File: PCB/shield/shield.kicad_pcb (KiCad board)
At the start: 2 copper layers, 128.2 x 80.1 mm, 19 parts, among them J1 QTR-8A, J10 ESP32_left_m, J11 ESP32_right_m, J13 Conn_01x06, J14 Domino, J15 Domino, J2 QMC5883L, J3 Servo, J4 Domino, J5 Joystick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

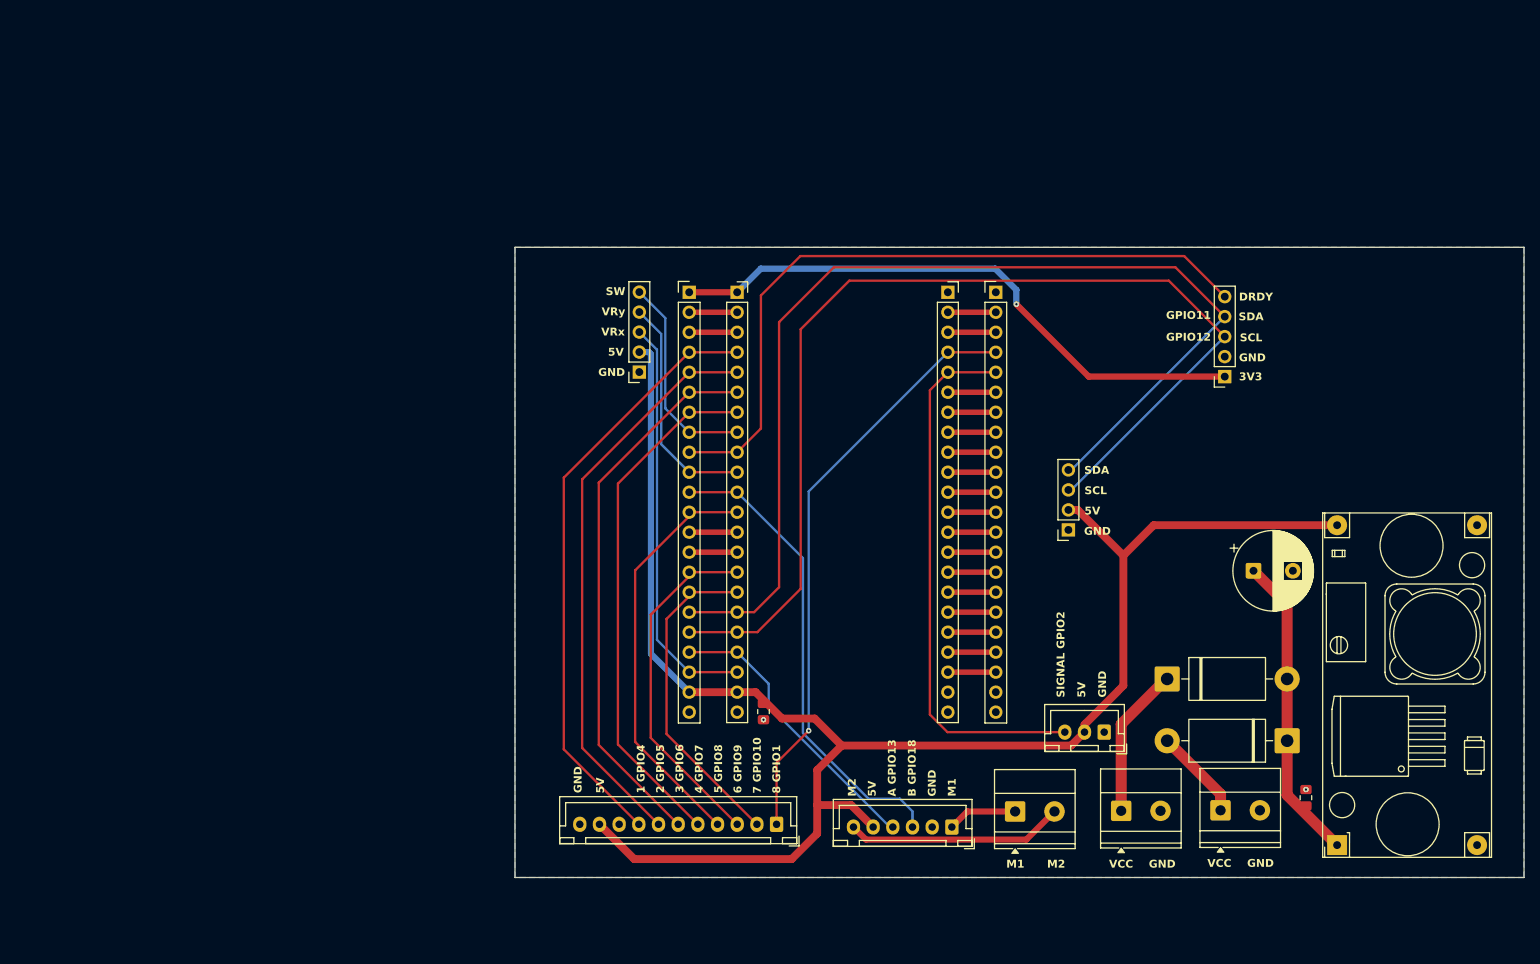
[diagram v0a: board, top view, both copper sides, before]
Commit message: feat: make pcb smaller
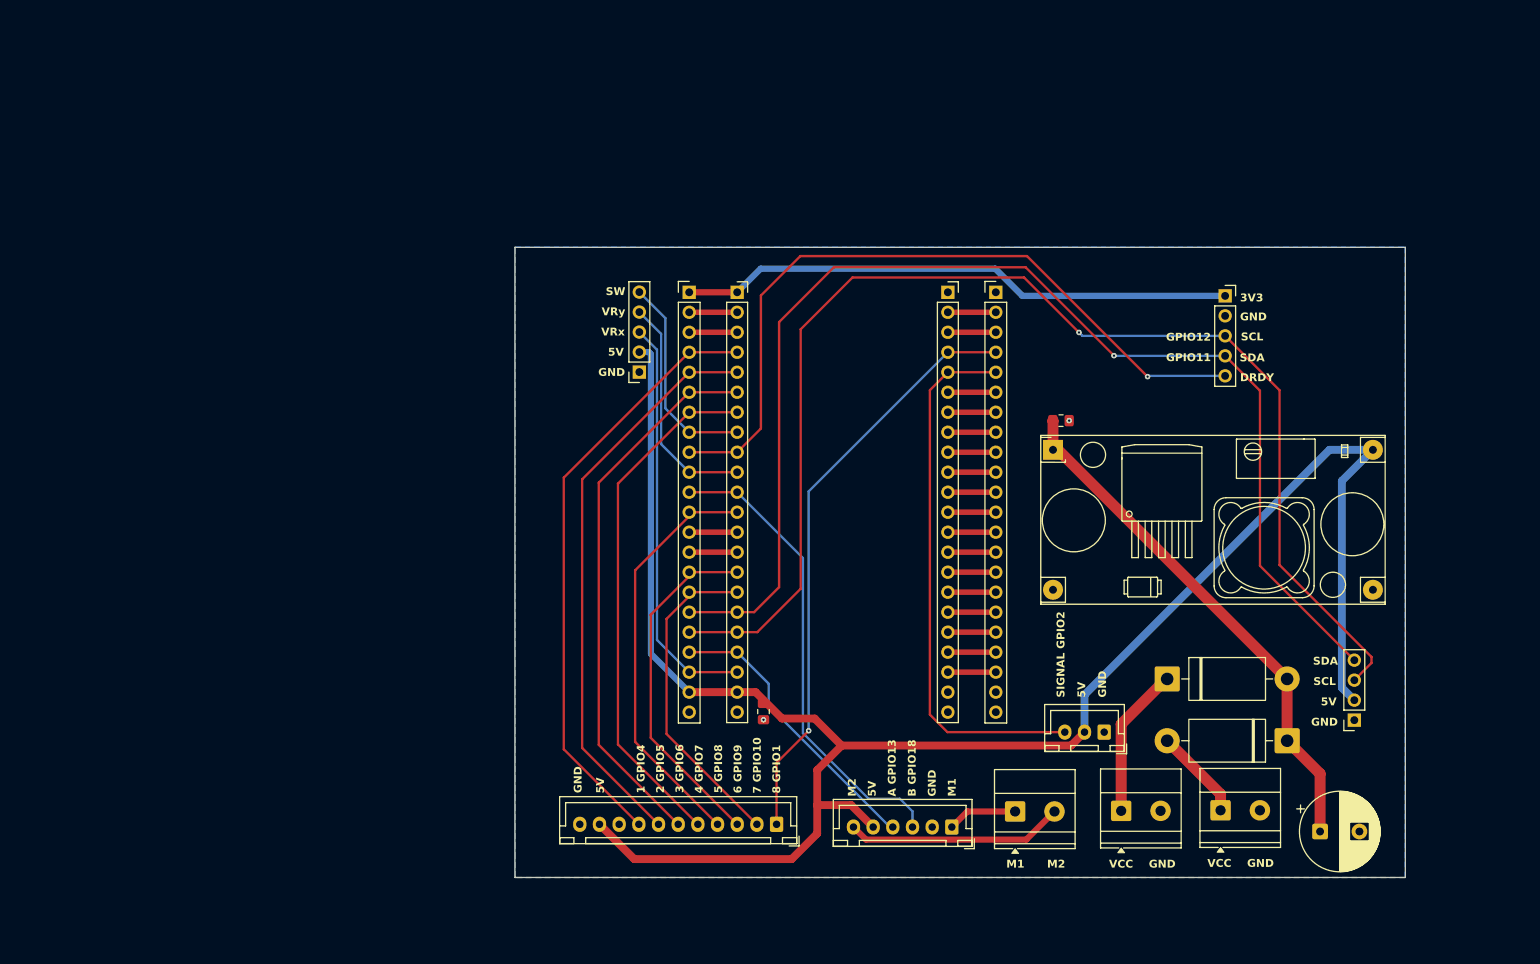
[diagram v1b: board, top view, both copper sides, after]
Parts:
- moved U1 61.8 mm to (155.9, 92.7), turned to 0 degrees
- moved C3 57.1 mm to (156.9, 89.0), turned to 0 degrees
- moved J6 43.6 mm to (194.2, 127.1)
- moved C1 34.2 mm to (189.9, 141.2)
- moved J2 10.3 mm to (177.8, 73.2), turned to 0 degrees
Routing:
- net VCC: track 39.2 -> 66.6 mm
- net +5V: track 214.2 -> 240.2 mm
- net /GPIO12+SCL: track 136.3 -> 161.5 mm, vias 0 -> 1
- net /GPIO11+SDA: track 136.1 -> 156.1 mm, vias 0 -> 1
- net +3V3: track 76.0 -> 70.8 mm, vias 1 -> 0
- net /GPIO16: track 90.4 -> 94.7 mm, vias 0 -> 1
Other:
- board size 128.2 x 80.1 mm -> 113.1 x 80.1 mm

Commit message: wip: commit to change workplace
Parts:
- removed J10: ESP32_left_m, Connector_PinHeader_2.54mm:PinHeader_1x22_P2.54mm_Vertical
- removed J11: ESP32_right_m, Connector_PinHeader_2.54mm:PinHeader_1x22_P2.54mm_Vertical
- removed J8: ESP32_left_f, Connector_PinSocket_2.54mm:PinSocket_1x22_P2.54mm_Vertical
- removed J9: ESP32_right_f, Connector_PinSocket_2.54mm:PinSocket_1x22_P2.54mm_Vertical
- added J7: L298N, Connector_JST:JST_XH_B3B-XH-A_1x03_P2.50mm_Vertical, F.Cu at (189.6, 76.3)
- added U2: ESP32-S3-DevKitC, PCM_Espressif:ESP32-S3-DevKitC, F.Cu at (156.8, 124.1)
- C3, C5: footprint Capacitor_SMD:C_0805_2012Metric_Pad1.18x1.45mm_HandSolder -> Capacitor_THT:CP_Radial_D5.0mm_P2.50mm
- moved C5 76.5 mm to (165.1, 64.9), turned to 0 degrees
- moved J6 63.9 mm to (187.5, 63.5), turned to 0 degrees
- moved J14 61.2 mm to (191.4, 92.6), turned to 90 degrees
- moved J5 55.4 mm to (127.7, 132.6), turned to 0 degrees
- moved J13 54.0 mm to (188.6, 111.6), turned to 90 degrees
- moved J1 49.0 mm to (169.8, 141.9)
- moved J2 45.8 mm to (187.4, 118.0), turned to 90 degrees
- moved C3 30.3 mm to (167.9, 117.3), turned to 180 degrees
- moved J3 27.8 mm to (138.0, 141.8)
- moved C1 24.3 mm to (171.0, 125.8), turned to 180 degrees
- moved U1 20.5 mm to (165.1, 111.0), turned to 90 degrees
- moved J15 14.1 mm to (178.6, 139.3)
- moved J4 13.6 mm to (190.8, 139.4)
- moved D2 11.2 mm to (178.1, 130.0)
- moved D1 10.0 mm to (193.5, 123.4)
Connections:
- net Net-(J13-Pin_1) renamed /M1
- net Net-(J13-Pin_6) renamed /M2
- D1 pad 1: VCC -> Net-(D1-K)
- D1 pad 2: Net-(D1-A) -> VCC
- D2 pad 1: Net-(D2-K) -> VCC
- D2 pad 2: VCC -> Net-(D2-A)
- J1 pad 1: /GPIO1 -> /GPIO4
- J1 pad 2: /GPIO10 -> /GPIO5
- J1 pad 3: /GPIO9 -> /GPIO6
- J1 pad 4: /GPIO8 -> /GPIO7
- J1 pad 5: /GPIO7 -> /GPIO8
- J1 pad 6: /GPIO6 -> /GPIO3
- J1 pad 7: /GPIO5 -> /GPIO9
- J1 pad 8: /GPIO4 -> /GPIO10
- J13 pad 3: /GPIO18 -> /GPIO17
- J13 pad 4: /GPIO13 -> /GPIO18
- J15 pad 1: Net-(D2-K) -> Net-(D1-K)
- J2 pad 3: /GPIO12+SCL -> /GPIO15
- J2 pad 4: /GPIO11+SDA -> /GPIO16
- J2 pad 5: /GPIO16 -> unconnected-(J2-Pin_5-Pad5)
- J3 pad 3: /GPIO2 -> /GPIO11
- J4 pad 1: Net-(D1-A) -> Net-(D2-A)
- J5 pad 3: /GPIO14 -> /GPIO2
- J5 pad 4: /GPIO17 -> /GPIO1
- J5 pad 5: /GPIO15 -> /GPIO12
- J6 pad 3: /GPIO12+SCL -> /GPIO15
- J6 pad 4: /GPIO11+SDA -> /GPIO16
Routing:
- net /GPIO12+SCL: track 161.5 -> 0.00 mm, vias 1 -> 0
- net /GPIO11+SDA: track 156.1 -> 0.00 mm, vias 1 -> 0
- net /GPIO15: track 26.5 -> 107.4 mm
- net /GPIO12: track 0.00 -> 76.9 mm
- net /GPIO11: track 0.00 -> 71.1 mm
- net /GPIO21: track 0.00 -> 56.8 mm
- net /GPIO3: track 0.00 -> 54.6 mm
- net /GPIO1: track 75.1 -> 26.3 mm, vias 1 -> 0
- net /GPIO4: track 76.6 -> 32.8 mm
- net /GPIO2: track 68.6 -> 26.3 mm
- net /GPIO5: track 73.2 -> 35.1 mm
- net VCC: track 66.6 -> 32.2 mm
- net /GPIO6: track 69.9 -> 37.4 mm
- net /GPIO7: track 66.4 -> 39.8 mm
- net /GPIO18: track 60.2 -> 34.0 mm
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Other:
- board size 113.1 x 80.1 mm -> 79.7 x 87.2 mm
- board text added: "1"
- board text added: "2"
- board text added: "3"
- board text added: "4"
- board text added: "5"
- board text added: "6"
- board text added: "7"
- board text added: "8"
- board text added: "A"
- board text added: "B"
- board text added: "EN"
- board text added: "IN1"
- board text added: "IN2"
- board text added: "JOYSTICK"
- board text added: "L298N"
- board text added: "MOTOR"
- board text added: "QMC5883L"
- board text added: "QTR-8A"
- board text added: "SCREEN"
- board text added: "SERVO"
- board text added: "SIGNAL"
- board text added: "Vin"
- board text added: "Vout"
- board text removed: "1 GPIO4"
- board text removed: "2 GPIO5"
- board text removed: "3 GPIO6"
- board text removed: "4 GPIO7"
- board text removed: "5 GPIO8"
- board text removed: "6 GPIO9"
- board text removed: "7 GPIO10"
- board text removed: "8 GPIO1"
- board text removed: "A GPIO13"
- board text removed: "B GPIO18"
- board text removed: "DRDY"
- board text removed: "GPIO11"
- board text removed: "GPIO12"
- board text removed: "SIGNAL GPIO2"
- board text removed: "VCC"

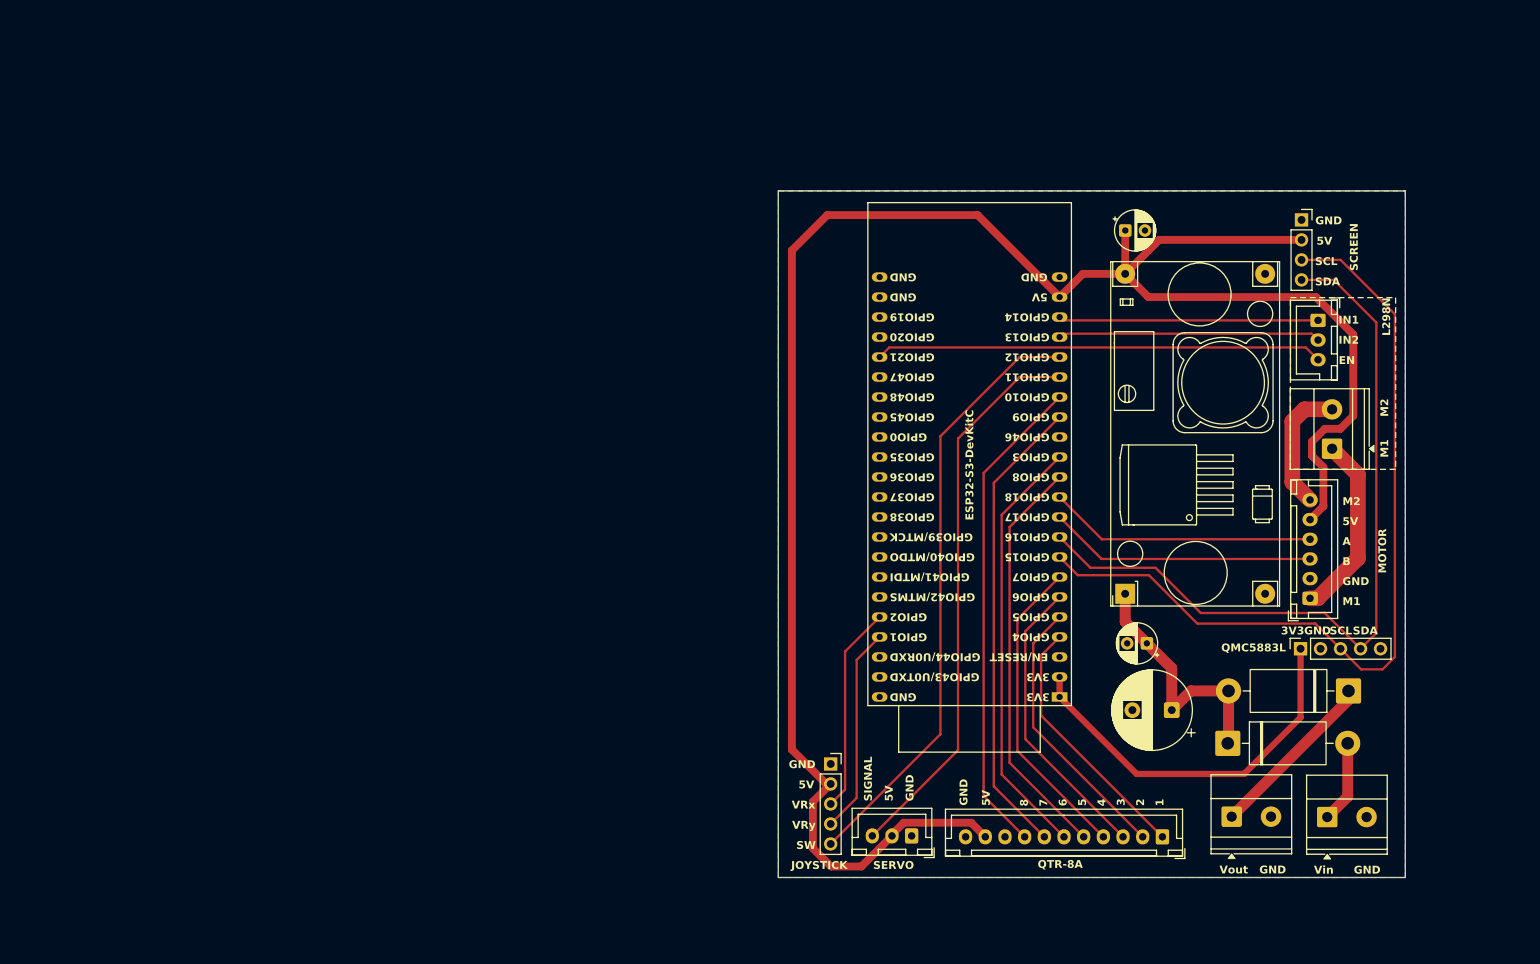
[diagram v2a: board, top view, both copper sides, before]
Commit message: feat: change pcb design, use tb6612fng for controlling motor and mosfet for reverse polar protection
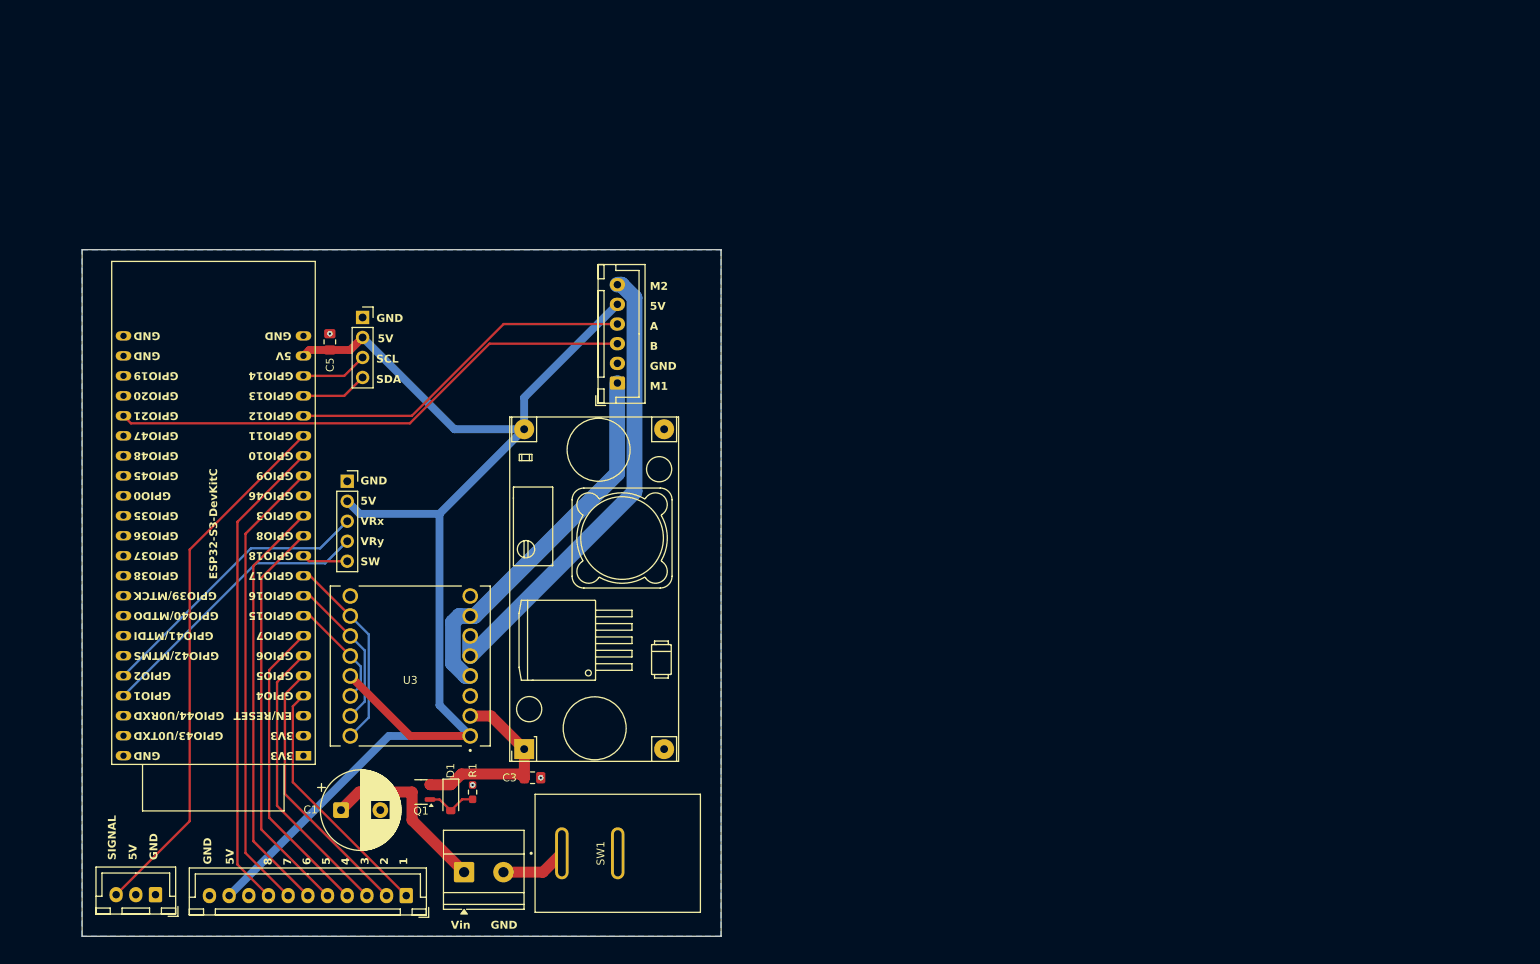
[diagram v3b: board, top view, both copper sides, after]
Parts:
- removed D2: 1N5822, Diode_THT:D_DO-201AD_P15.24mm_Horizontal
- removed J14, J15: Domino, TerminalBlock_Phoenix:TerminalBlock_Phoenix_MKDS-1,5-2_1x02_P5.00mm_Horizontal
- removed J2: QMC5883L, Connector_PinSocket_2.54mm:PinSocket_1x05_P2.54mm_Vertical
- removed J7: L298N, Connector_JST:JST_XH_B3B-XH-A_1x03_P2.50mm_Vertical
- added Q1: SI2301DS, Package_TO_SOT_SMD:SOT-23-3, F.Cu at (75.6, 136.2)
- added R1: 10k, Resistor_SMD:R_0603_1608Metric_Pad0.98x0.95mm_HandSolder, F.Cu at (82.2, 136.2)
- added SW1: SW_SPST, Rocket Switch:SW_RF1-1A-DC-2-R-1, F.Cu at (100.6, 144.0)
- added U3: TB6612FNG, TB6612FNG:MODULE_ROB-14450, F.Cu at (74.3, 120.2)
- C3, C5: footprint Capacitor_THT:CP_Radial_D5.0mm_P2.50mm -> Capacitor_SMD:C_0805_2012Metric_Pad1.18x1.45mm_HandSolder
- D1: value 1N5822 -> BZT52C5V1; footprint Diode_THT:D_DO-201AD_P15.24mm_Horizontal -> Diode_SMD:D_SOD-123
- J13: value Conn_01x06 -> Motor
- J4: value Domino -> Battery
- U1: value YAAJ_DCDC_StepDown_LM2596 -> LM2596
- moved J6 119.9 mm to (68.2, 75.9)
- moved D1 114.8 mm to (79.4, 136.9), turned to -90 degrees
- moved J4 109.9 mm to (81.1, 146.4)
- moved C1 106.3 mm to (65.5, 138.5), turned to 0 degrees
- moved C5 102.0 mm to (64.1, 79.0), turned to 90 degrees
- moved J3 96.4 mm to (41.9, 149.3)
- moved J1 96.4 mm to (73.8, 149.4)
- moved U2 96.4 mm to (60.7, 131.6)
- moved J13 92.1 mm to (100.6, 84.3)
- moved C3 79.9 mm to (89.8, 134.4), turned to 0 degrees
- moved U1 78.9 mm to (88.7, 130.8)
- moved J5 71.1 mm to (66.3, 96.7)
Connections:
- C1 pad 1: VCC -> Net-(J4-Pin_1)
- D1 pad 1: Net-(D1-K) -> VCC
- D1 pad 2: VCC -> Net-(D1-A)
- J13 pad 3: /GPIO17 -> /GPIO21
- J13 pad 4: /GPIO18 -> /GPIO12
- J4 pad 1: Net-(D2-A) -> Net-(J4-Pin_1)
- J4 pad 2: GND -> Net-(J4-Pin_2)
- J5 pad 5: /GPIO12 -> /GPIO18
- J6 pad 3: /GPIO15 -> /GPIO14
- J6 pad 4: /GPIO16 -> /GPIO13
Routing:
- net /GPIO15: track 107.4 -> 14.3 mm
- net /GPIO16: track 98.1 -> 19.8 mm
- net +5V: track 245.0 -> 169.5 mm
- net +3V3: track 48.9 -> 0.00 mm
- net /M2: track 16.6 -> 59.6 mm
- net /GPIO12: track 76.9 -> 44.7 mm
- net /GPIO18: track 34.0 -> 5.85 mm
- net /GPIO13: track 33.3 -> 8.49 mm
- net /M1: track 23.5 -> 48.3 mm
- net /GPIO14: track 33.0 -> 8.48 mm
- net Net-(J4-Pin_1): track 0.00 -> 22.9 mm
- net Net-(D1-K): track 22.1 -> 0.00 mm
- net /GPIO21: track 56.8 -> 67.3 mm
- net Net-(D2-A): track 10.4 -> 0.00 mm
- net /GPIO2: track 26.3 -> 36.6 mm
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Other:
- board size 79.7 x 87.2 mm -> 81.2 x 87.2 mm
- board text removed: "3V3"
- board text removed: "EN"
- board text removed: "IN1"
- board text removed: "IN2"
- board text removed: "JOYSTICK"
- board text removed: "L298N"
- board text removed: "MOTOR"
- board text removed: "QMC5883L"
- board text removed: "QTR-8A"
- board text removed: "SCREEN"
- board text removed: "SERVO"
- board text removed: "Vout"
